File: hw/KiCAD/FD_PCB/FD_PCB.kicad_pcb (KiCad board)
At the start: 2 copper layers, 212.8 x 126.7 mm, 143 parts, among them J1 Barrel_Jack_Switch, J10 Conn_01x02, J11 Conn_01x02, J12 Conn_01x02, J13 Conn_02x10_Odd_Even, J14 MQ-4 Gas Sensor, J15 MQ-7 Gas Sensor, J16 MQ-138 Gas Sensor, J17 KY-026 Flame Sensor, J18 Conn_01x10, J19 Conn_01x05, J2 Conn_02x12_Odd_Even, J20 HDC3022, J21 Conn_01x08, J22 MiCS-6814, J23 Conn_01x02, J3 Conn_02x12_Odd_Even, J4 Conn_02x20_Odd_Even, J5 Conn_02x10_Odd_Even, J6 Conn_01x07, J7 Conn_01x02, J8 Conn_01x08, J9 Conn_01x16, M1 Motor_Servo, M2 Motor_Servo, SW1 SW_Push, SW2 SW_Push, SW3 SW_Push, U1 ADS1115IDGS, U2 OPA2350, U3 OPA2350, U4 ADS1115IDGS

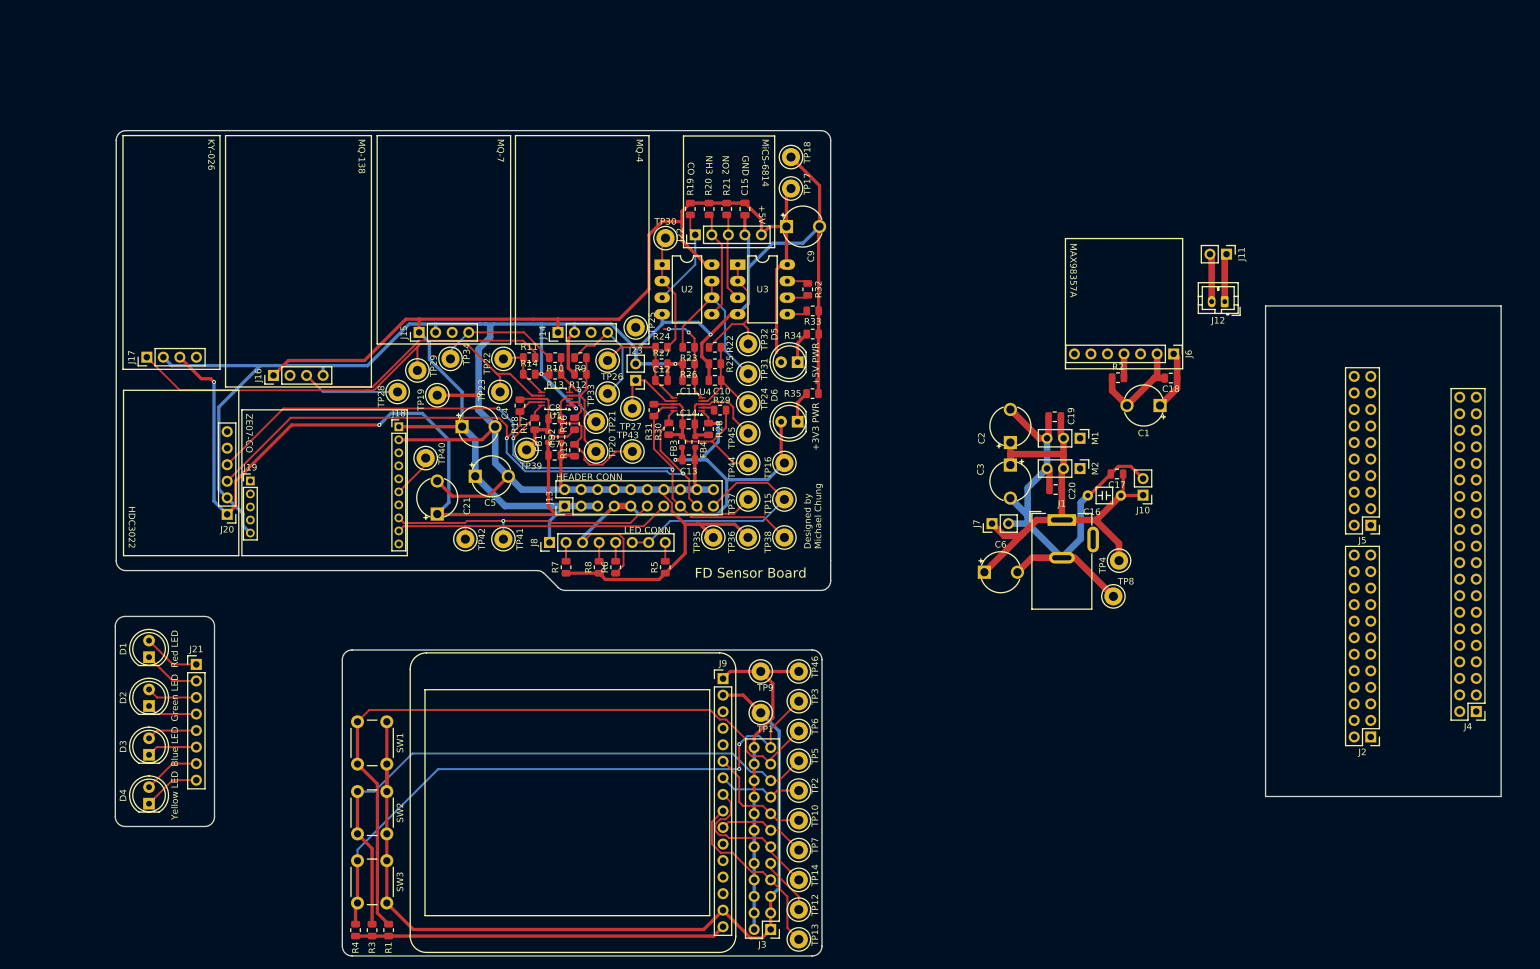
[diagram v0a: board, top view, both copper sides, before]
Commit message: finish sensor board, lcd board, led board, and header board
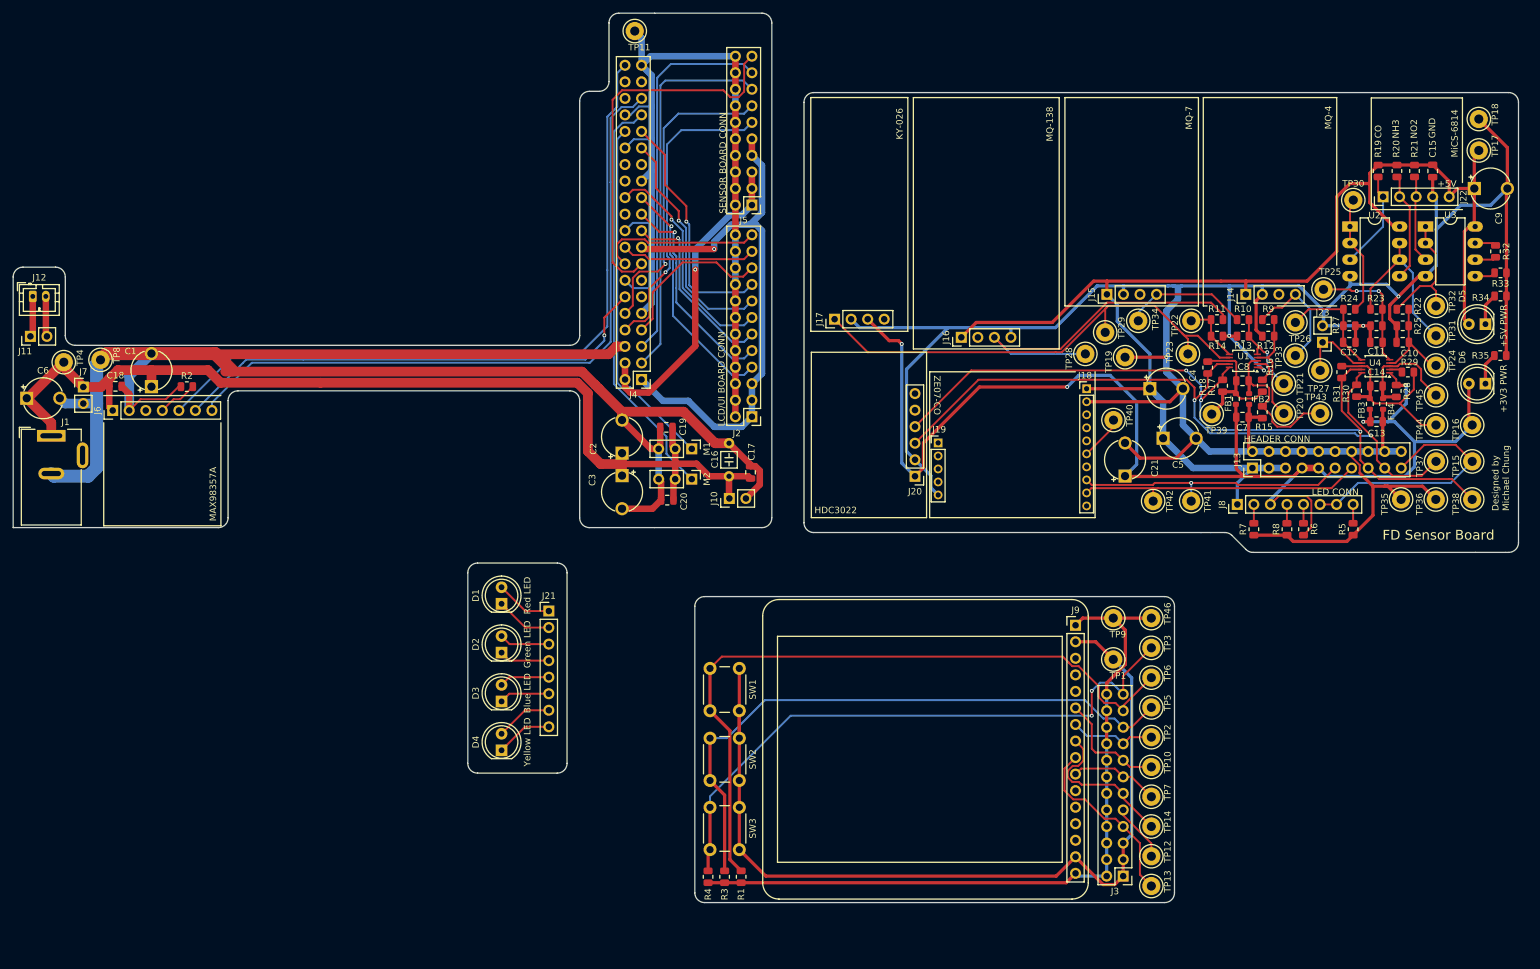
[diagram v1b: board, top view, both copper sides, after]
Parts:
- added TP11: TestPoint, TestPoint:TestPoint_Loop_D3.50mm_Drill1.4mm_Beaded, F.Cu at (95.5, 2.74)
- moved J11 184.1 mm to (2.64, 49.6), turned to 90 degrees
- moved J12 183.0 mm to (3.01, 43.5), turned to 0 degrees
- moved TP4 164.9 mm to (7.77, 53.6), turned to 90 degrees
- moved J6 163.2 mm to (15.3, 61.0), turned to 90 degrees
- moved C18 162.1 mm to (15.7, 57.3), turned to 0 degrees
- moved TP8 159.7 mm to (13.4, 53.2), turned to 90 degrees
- moved J1 155.7 mm to (5.85, 64.9)
- moved C1 154.9 mm to (21.2, 57.4), turned to 90 degrees
- moved C6 149.5 mm to (2.08, 59.1)
- moved R2 143.0 mm to (26.7, 57.4)
- moved J7 141.1 mm to (10.8, 57.4), turned to 0 degrees
- moved J4 138.0 mm to (96.5, 56.3)
- moved J2 107.0 mm to (113.4, 62.0)
- moved J5 107.0 mm to (113.4, 29.5)
- moved C7 105.8 mm to (188.8, 62.0)
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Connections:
- C1 pad 2: GND -> EXT_GND
- C16 pad 2: GND -> EXT_GND
- C17 pad 2: GND -> EXT_GND
- C18 pad 2: GND -> EXT_GND
- C19 pad 2: GND -> EXT_GND
- C2 pad 2: GND -> EXT_GND
- C20 pad 2: GND -> EXT_GND
- C3 pad 2: GND -> EXT_GND
- C6 pad 2: GND -> EXT_GND
- J1 pad 2: GND -> EXT_GND
- J10 pad 2: GND -> EXT_GND
- J4 pad 6: GND -> EXT_GND
- J6 pad 2: GND -> EXT_GND
- J7 pad 2: GND -> EXT_GND
- M1 pad 3: GND -> EXT_GND
- M2 pad 3: GND -> EXT_GND
- R2 pad 1: GND -> EXT_GND
- TP8 pad 1: GND -> EXT_GND
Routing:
- net EXT_GND: track 0.00 -> 260.0 mm
- net I2S0_DOUT: track 0.00 -> 112.4 mm
- net I2S0_FS: track 0.00 -> 106.7 mm
- net +3V3: track 0.00 -> 85.6 mm, vias 0 -> 1
- net +5V_EXT: track 83.2 -> 162.0 mm
- net I2S0_SCK: track 0.00 -> 75.3 mm, vias 0 -> 1
- net GPIO13: track 0.00 -> 63.6 mm
- net I2C1_SDA: track 0.00 -> 58.7 mm
- net I2C1_SCL: track 0.00 -> 58.2 mm
- net GPIO12: track 0.00 -> 58.0 mm
- net GPIO07: track 0.00 -> 54.7 mm
- net +5V: track 0.00 -> 49.3 mm, vias 0 -> 1
- net UART1_RXD: track 0.00 -> 47.8 mm, vias 0 -> 1
- net UART1_TXD: track 0.00 -> 46.9 mm, vias 0 -> 1
- net GPIO11: track 0.00 -> 37.2 mm, vias 0 -> 1
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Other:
- board size 212.8 x 126.7 mm -> 231.2 x 136.6 mm
- board text added: "LCD/UI BOARD CONN"
- board text added: "SENSOR BOARD CONN"
